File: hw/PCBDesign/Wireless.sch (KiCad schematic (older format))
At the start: 29 parts, among them Q2 2N7002, Q3 2N7002, Q4 LBSS84LT1G, Q5 LBSS84LT1G, U14 RN4871, U6 NRF24L01_Breakout

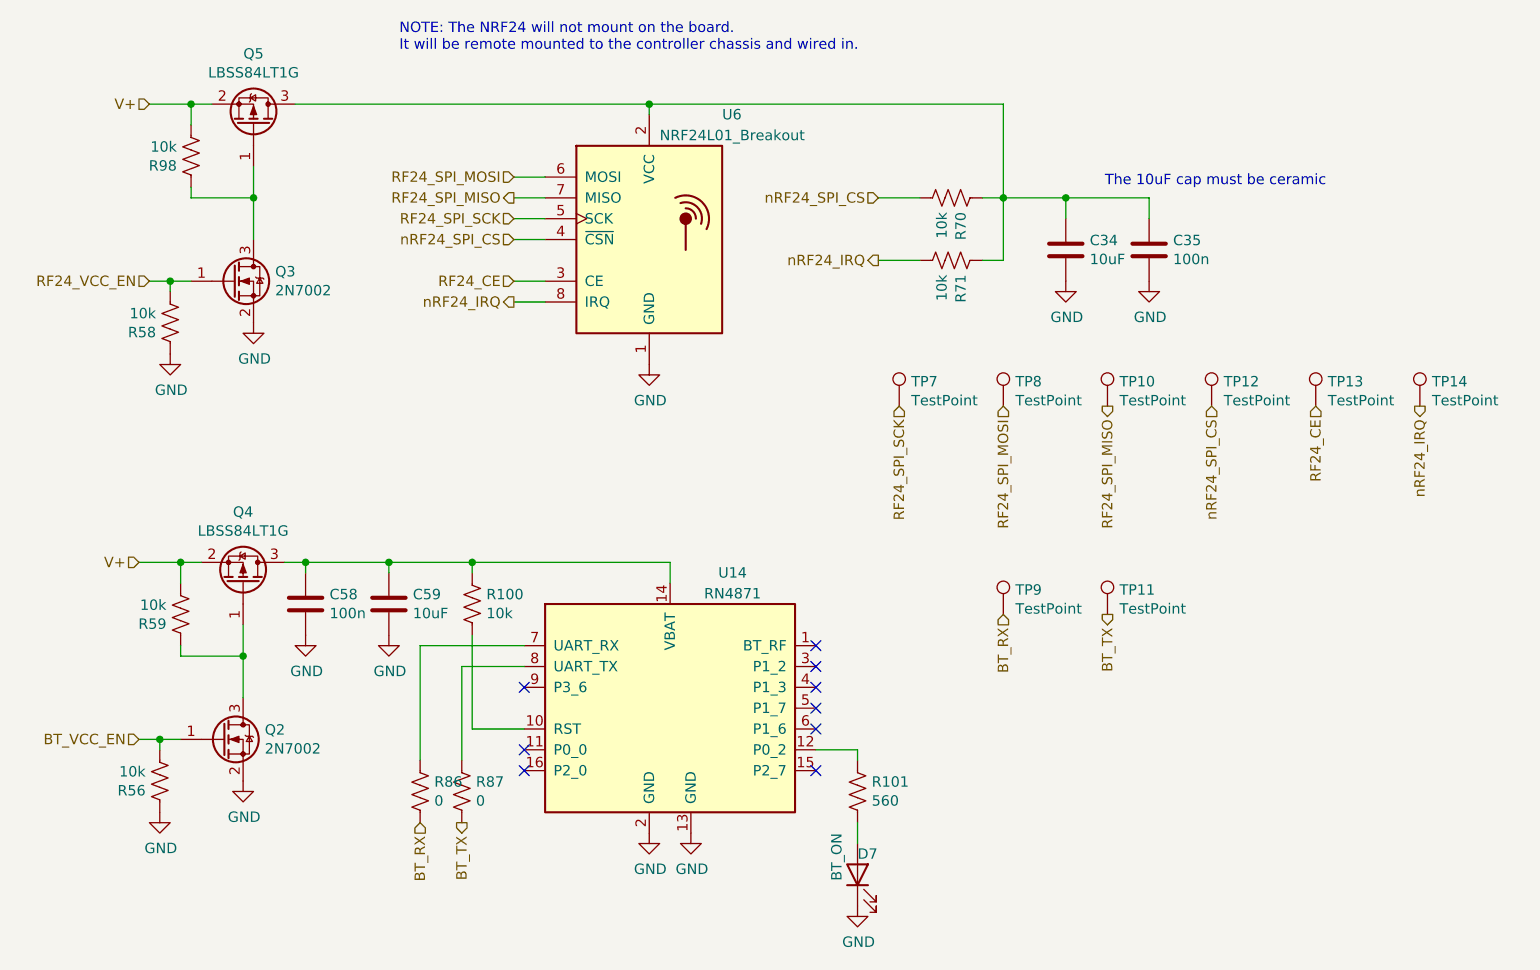
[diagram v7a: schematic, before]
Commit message: Start working on PCB rev 2.0
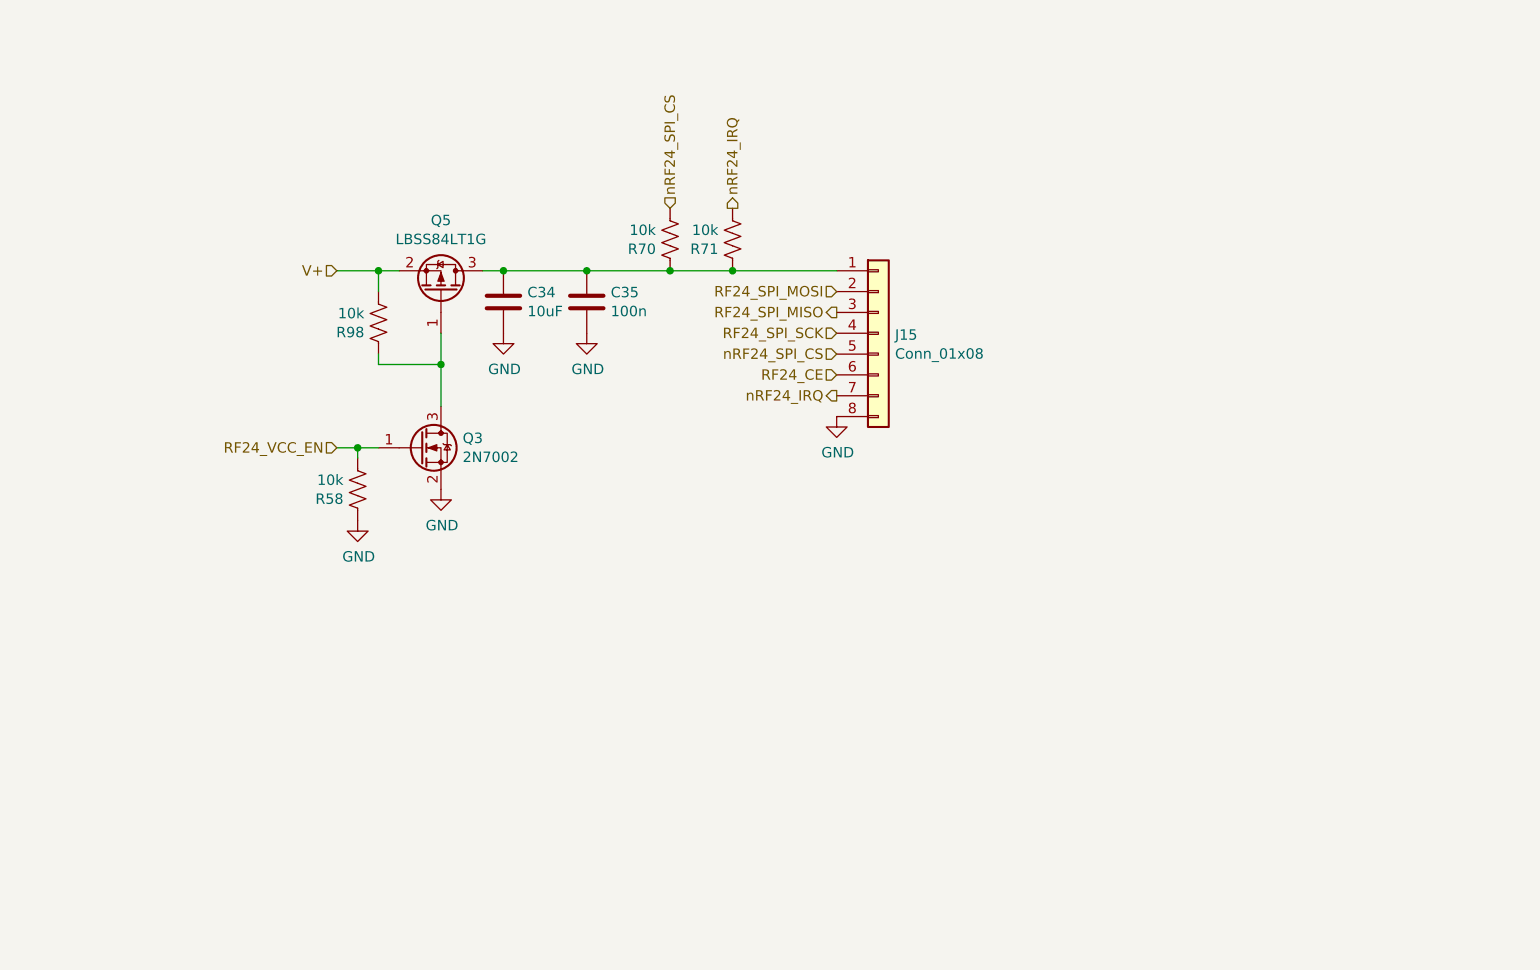
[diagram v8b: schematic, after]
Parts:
- removed C58: 100n, Capacitor_SMD:C_0402_1005Metric, symbol Device:C
- removed C59: 10uF, Capacitor_SMD:C_0805_2012Metric, symbol Device:C
- removed D7: BT_ON, LED_SMD:LED_0603_1608Metric, symbol Device:LED
- removed Q2: 2N7002, Package_TO_SOT_SMD:SOT-23, symbol Transistor_FET:2N7002
- removed Q4: LBSS84LT1G, Package_TO_SOT_SMD:SOT-23, symbol Transistor_FET:Si2319CDS
- removed R100, R56, R59: 10k, Resistor_SMD:R_0402_1005Metric, symbol Device:R_US
- removed R101: 560, Resistor_SMD:R_0402_1005Metric, symbol Device:R_US
- removed R86, R87: 0, Resistor_SMD:R_0805_2012Metric, symbol Device:R_US
- removed TP10, TP11, TP12, TP13, TP14, TP7, TP8, TP9: TestPoint, TestPoint:TestPoint_Pad_2.5x2.5mm, symbol Connector:TestPoint
- removed U14: RN4871, RF_Module:Microchip_RN4871, symbol RF_Bluetooth:RN4871
- removed U6: NRF24L01_Breakout, RF_Module:nRF24L01_Breakout, symbol RF:NRF24L01_Breakout
- added J15: Conn_01x08, Connector_Molex:Molex_PicoBlade_53261-0871_1x08-1MP_P1.25mm_Horizontal, symbol Connector_Generic:Conn_01x08
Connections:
- net GND: now also J15.8 (Pin_8)
- net RF24_CE: now also J15.6 (Pin_6)
- net RF24_SPI_MISO: now also J15.3 (Pin_3)
- net RF24_SPI_MOSI: now also J15.2 (Pin_2)
- net RF24_SPI_SCK: now also J15.4 (Pin_4)
- net nRF24_IRQ: now also J15.7 (Pin_7)
- net nRF24_SPI_CS: now also J15.5 (Pin_5)
- net at C34.1, C35.1, Q5.3 (D)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: now also J15.1 (Pin_1)
- no-connect marks 9 -> 0
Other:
- note removed: "NOTE: The NRF24 will not mount on the board.\nIt will be remote mounted to the controller chassis and wired in."
- note removed: "The 10uF cap must be ceramic"
- moved on the sheet: C34, C35, Q3, Q5, R58, R70, R71, R98
